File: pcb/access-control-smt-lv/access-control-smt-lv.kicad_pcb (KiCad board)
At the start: 2 copper layers, 69.8 x 33.8 mm, 25 parts, among them U1 ESP32-WROOM-E

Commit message: Mostly done SMT controller
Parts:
- added C1: 0.1U, Capacitor_SMD:C_1808_4520Metric_Pad1.72x2.30mm_HandSolder, F.Cu at (26.9, 3.52)
- added CON_3v3: Conn_01x02_Socket, Connector_PinHeader_2.54mm:PinHeader_1x02_P2.54mm_Vertical, F.Cu at (33.9, 1.74)
- added CON_5v1: Conn_01x02_Socket, Connector_PinHeader_2.54mm:PinHeader_1x02_P2.54mm_Vertical, F.Cu at (82.2, 21.4)
- added CON_AUX1: Conn_01x04_Socket, Connector_PinHeader_2.54mm:PinHeader_1x04_P2.54mm_Vertical, F.Cu at (35.5, 11.8)
- added R_EN1: 10kR, Resistor_SMD:R_2010_5025Metric_Pad1.40x2.65mm_HandSolder, F.Cu at (33.1, 5.84)
- PAD_SWL1, PAD_SWS1: footprint Connector_Wire:SolderWirePad_1x01_SMD_5x10mm -> Connector_Wire:SolderWirePad_1x01_SMD_1x2mm
- R_BUTTON_PD1, R_LED1, R_Q_LED1, R_Q_RELAY1: footprint Resistor_SMD:R_1210_3225Metric_Pad1.30x2.65mm_HandSolder -> Resistor_SMD:R_2010_5025Metric_Pad1.40x2.65mm_HandSolder
- moved SW_BOOT1 1.46 mm to (19.2, 5.40)
- moved R_BUTTON_PD1 1.09 mm to (68.8, 22.7)
- moved R_Q_LED1 1.03 mm to (75.0, 5.45)
- moved PAD_SWL1 0.90 mm to (29.8, 15.7), turned to 90 degrees
- moved PAD_SWS1 0.81 mm to (38.8, 15.7), turned to -90 degrees
- moved R_LED1 0.74 mm to (76.2, 8.77)
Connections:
- U1 pad 8: unconnected-(U1-32K_XP/GPIO32/ADC1_CH4-Pad8) -> Net-(CON_AUX1-Pin_4)
- U1 pad 9: unconnected-(U1-32K_XN/GPIO33/ADC1_CH5-Pad9) -> Net-(CON_AUX1-Pin_3)
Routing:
- net GND: track 207.5 -> 272.5 mm, vias 2 -> 5
- net Net-(U1-GPIO0/BOOT/ADC2_CH1): track 64.6 -> 78.8 mm
- net Net-(CON_SENSE1-Pin_3): track 52.4 -> 42.0 mm
- net +3V3: track 124.3 -> 132.5 mm
- net Net-(CON_AUX1-Pin_3): track 0.00 -> 7.86 mm
- net Net-(U1-EN/CHIP_PU): track 34.0 -> 41.1 mm
- net Net-(CON_AUX1-Pin_4): track 0.00 -> 4.01 mm
- net Net-(CON_SENSE1-Pin_4): track 45.3 -> 48.0 mm
- net Net-(J_RELAY1-Pin_3): track 26.0 -> 23.3 mm
- net Net-(J_LED1-Pin_3): track 26.4 -> 28.2 mm
- net Net-(J_BUTTON1-Pin_1): track 52.6 -> 51.1 mm
- net Net-(Q_RELAY1-B): track 7.58 -> 6.77 mm
- net +5V: track 83.8 -> 84.5 mm
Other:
- outline, holes or cut-outs redrawn

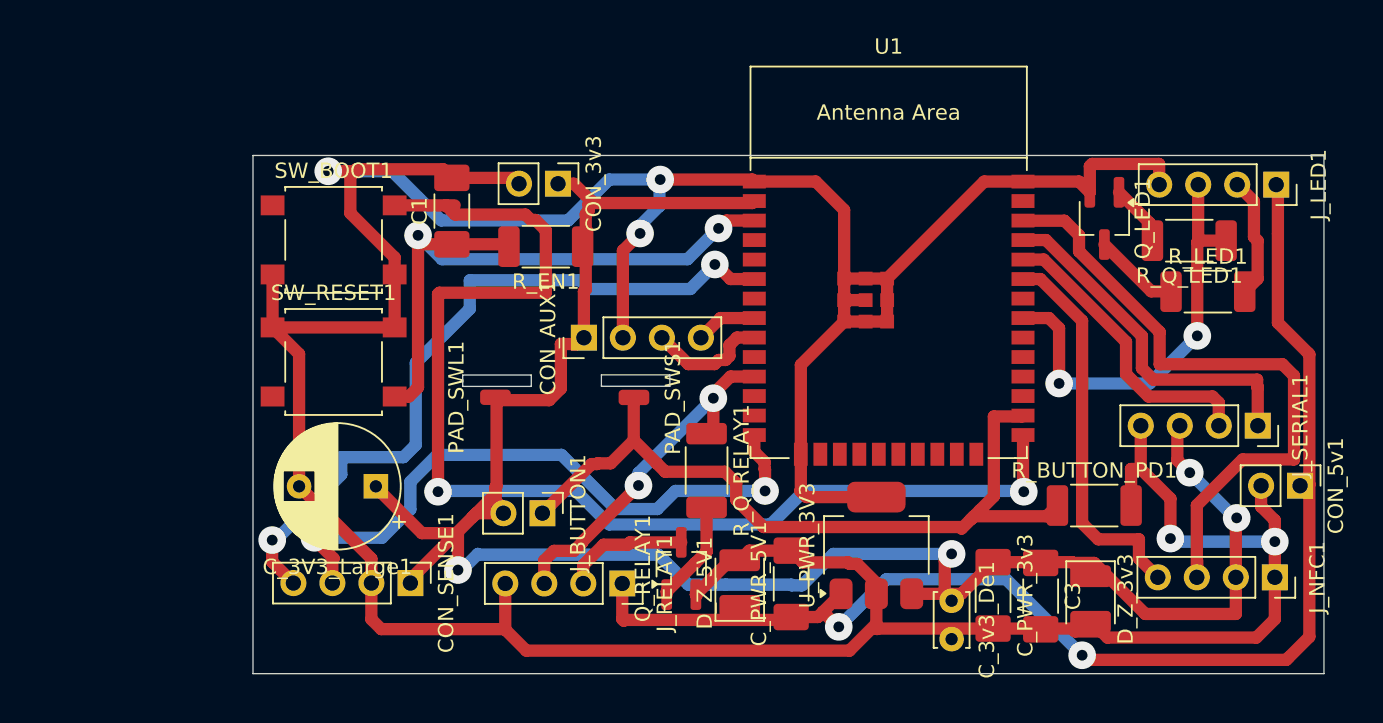
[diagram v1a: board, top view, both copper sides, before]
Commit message: NFC Clamp and progress with contactor interface
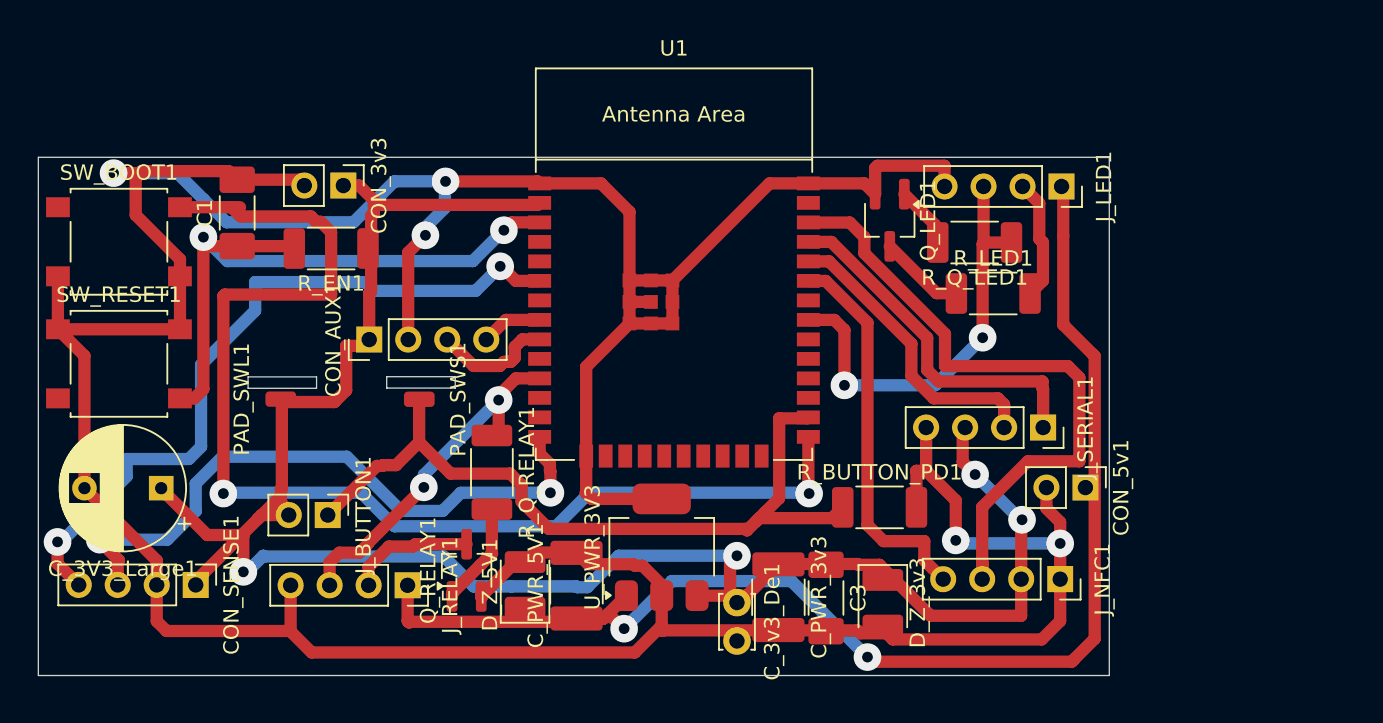
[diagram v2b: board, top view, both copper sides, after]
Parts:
- C_PWR_3v3, C_PWR_5V1: footprint Capacitor_SMD:C_1808_4520Metric_Pad1.72x2.30mm_HandSolder -> Capacitor_SMD:C_1812_4532Metric_Pad1.57x3.40mm_HandSolder
- moved C_PWR_3v3 14.0 mm to (48.2, 28.7)
- moved D_Z_5V1 14.0 mm to (31.7, 27.9)
- moved J_LED1 14.0 mm to (66.7, 1.92)
- moved J_NFC1 14.0 mm to (66.6, 27.5)
- moved J_SERIAL1 14.0 mm to (65.5, 17.6)
- moved PAD_SWS1 14.0 mm to (24.8, 15.8)
- moved Q_LED1 14.0 mm to (55.5, 4.12)
- moved R_BUTTON_PD1 14.0 mm to (54.8, 22.8)
- moved R_Q_LED1 14.0 mm to (61.0, 5.57)
- moved U_PWR_3V3 14.0 mm to (40.6, 25.4)
- moved CON_3v3 14.0 mm to (19.9, 1.86)
- moved CON_SENSE1 14.0 mm to (10.3, 27.9)
- moved C_3V3_Large1 14.0 mm to (8.02, 21.6)
- moved J_BUTTON1 14.0 mm to (18.9, 23.3)
- moved R_EN1 14.0 mm to (19.1, 5.96)
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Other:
- outline, holes or cut-outs redrawn

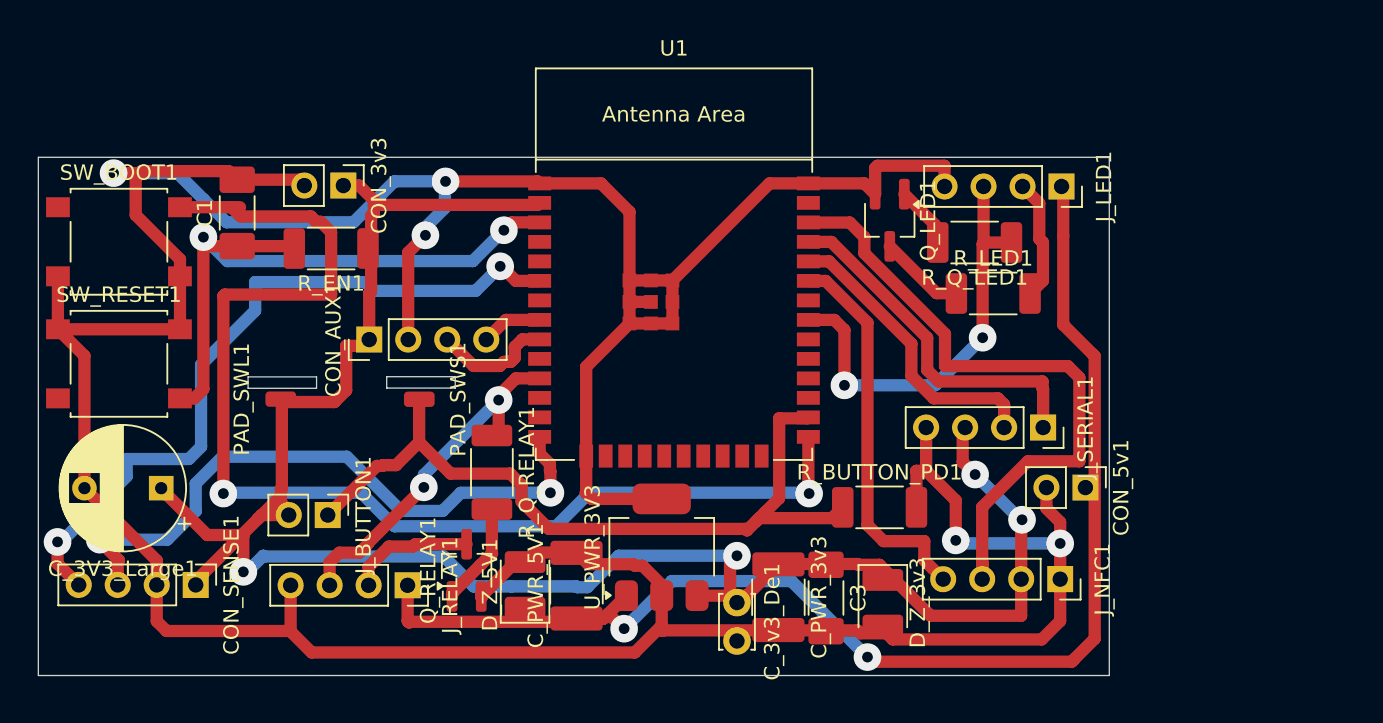
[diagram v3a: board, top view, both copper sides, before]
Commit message: Further optimisation of SMT version
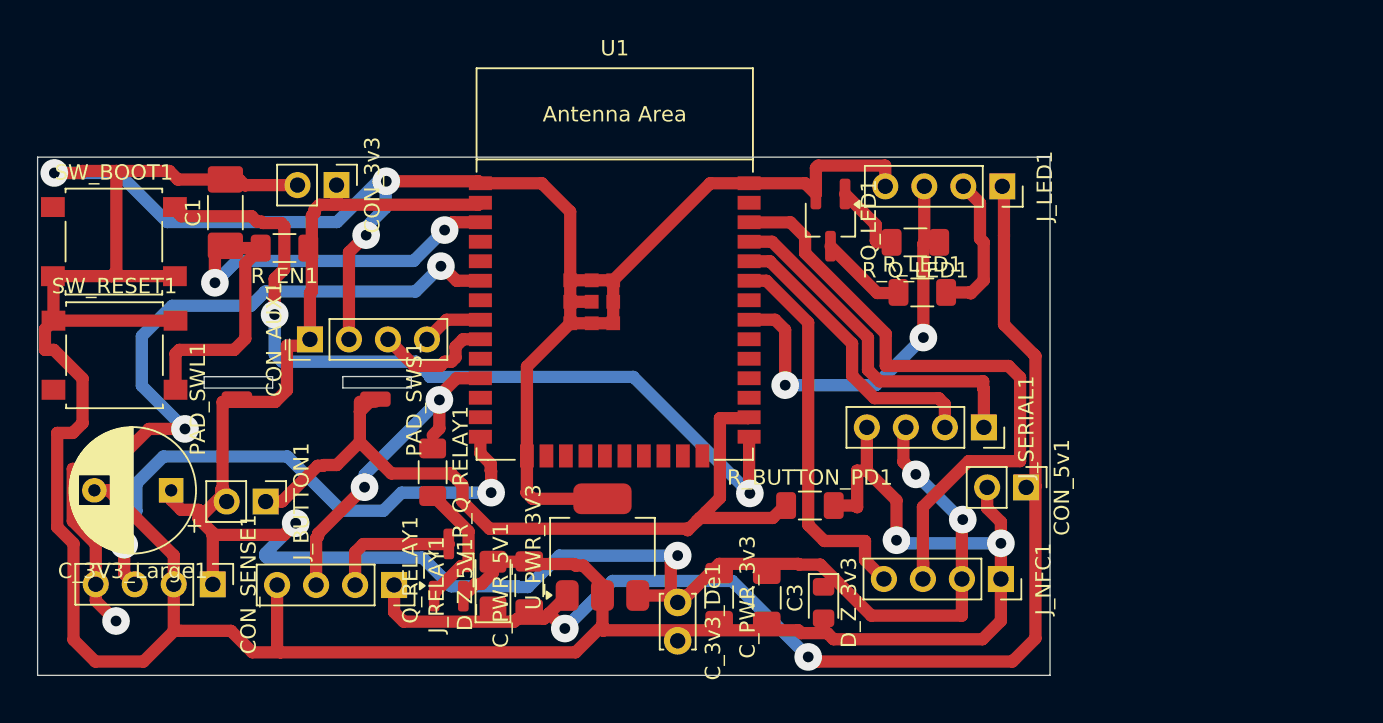
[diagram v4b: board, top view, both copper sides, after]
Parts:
- C3: footprint Capacitor_SMD:C_1808_4520Metric_Pad1.72x2.30mm_HandSolder -> Capacitor_SMD:C_1206_3216Metric_Pad1.33x1.80mm_HandSolder
- C_PWR_3v3, C_PWR_5V1: footprint Capacitor_SMD:C_1812_4532Metric_Pad1.57x3.40mm_HandSolder -> Capacitor_SMD:C_1206_3216Metric_Pad1.33x1.80mm_HandSolder
- D_Z_3v3: footprint Diode_SMD:D_1210_3225Metric_Pad1.42x2.65mm_HandSolder -> Diode_SMD:D_0805_2012Metric_Pad1.15x1.40mm_HandSolder
- D_Z_5V1: footprint Diode_SMD:D_1210_3225Metric_Pad1.42x2.65mm_HandSolder -> Diode_SMD:D_1206_3216Metric_Pad1.42x1.75mm_HandSolder
- R_BUTTON_PD1, R_EN1, R_LED1, R_Q_LED1, R_Q_RELAY1: footprint Resistor_SMD:R_2010_5025Metric_Pad1.40x2.65mm_HandSolder -> Resistor_SMD:R_1206_3216Metric_Pad1.30x1.75mm_HandSolder
- moved R_LED1 4.62 mm to (57.6, 8.82)
- moved R_BUTTON_PD1 4.54 mm to (50.3, 22.7)
- moved J_BUTTON1 4.14 mm to (14.8, 22.4)
- moved C_3v3_De1 3.86 mm to (41.7, 29.0)
- moved D_Z_3v3 3.86 mm to (51.2, 29.0)
- moved C3 3.86 mm to (47.5, 28.7)
- moved CON_5v1 3.86 mm to (64.4, 21.5)
- moved CON_AUX1 3.86 mm to (17.7, 11.9)
- moved C_PWR_3v3 3.86 mm to (44.4, 28.7)
- moved J_LED1 3.86 mm to (62.8, 1.91)
- moved Q_LED1 3.86 mm to (51.6, 4.11)
- moved R_Q_LED1 3.86 mm to (57.1, 5.56)
- moved R_Q_RELAY1 3.86 mm to (25.7, 20.5)
- moved U1 3.86 mm to (37.6, 8.72)
- moved U_PWR_3V3 3.86 mm to (36.8, 25.4)
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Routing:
- net Net-(U1-GPIO0/BOOT/ADC2_CH1): track 78.8 -> 55.7 mm
- net GND: track 272.5 -> 295.4 mm
- net +3V3: track 132.5 -> 125.8 mm
- net Net-(CON_SENSE1-Pin_3): track 42.0 -> 37.2 mm
- net +5V: track 84.5 -> 81.1 mm
- net Net-(U1-EN/CHIP_PU): track 41.1 -> 37.8 mm
- net Net-(CON_SENSE1-Pin_4): track 48.0 -> 51.0 mm, vias 2 -> 3
- net Net-(J_RELAY1-Pin_3): track 23.3 -> 21.3 mm
- net Net-(Q_RELAY1-B): track 6.77 -> 8.72 mm
- net Net-(J_LED1-Pin_2): track 7.87 -> 9.50 mm
- net Net-(J_BUTTON1-Pin_1): track 51.1 -> 52.2 mm
- net Net-(Q_LED1-B): track 4.08 -> 4.95 mm
- net Net-(J_LED1-Pin_3): track 28.2 -> 27.4 mm
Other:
- board size 69.8 x 33.8 mm -> 65.9 x 33.8 mm
